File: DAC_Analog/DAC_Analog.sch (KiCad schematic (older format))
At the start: 0 parts

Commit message: Update dac analog design
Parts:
- added U?: ISO154x, symbol ISO154x
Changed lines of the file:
@@
 Text Notes 8550 3900 0    79   ~ 0
 Digital \nsource converter\n &\nDAC
+$Comp
+L ISO154x U?
+U 1 1 59C5CEDC
+P 4850 4050
+F 0 "U?" H 4600 4500 60  0000 C CNN
+F 1 "ISO154x" H 4950 3600 60  0000 C CNN
+F 2 "" H 4850 4050 60  0001 C CNN
+F 3 "" H 4850 4050 60  0001 C CNN
+	1    4850 4050
+	1    0    0    -1
+$EndComp
 $EndSCHEMATC

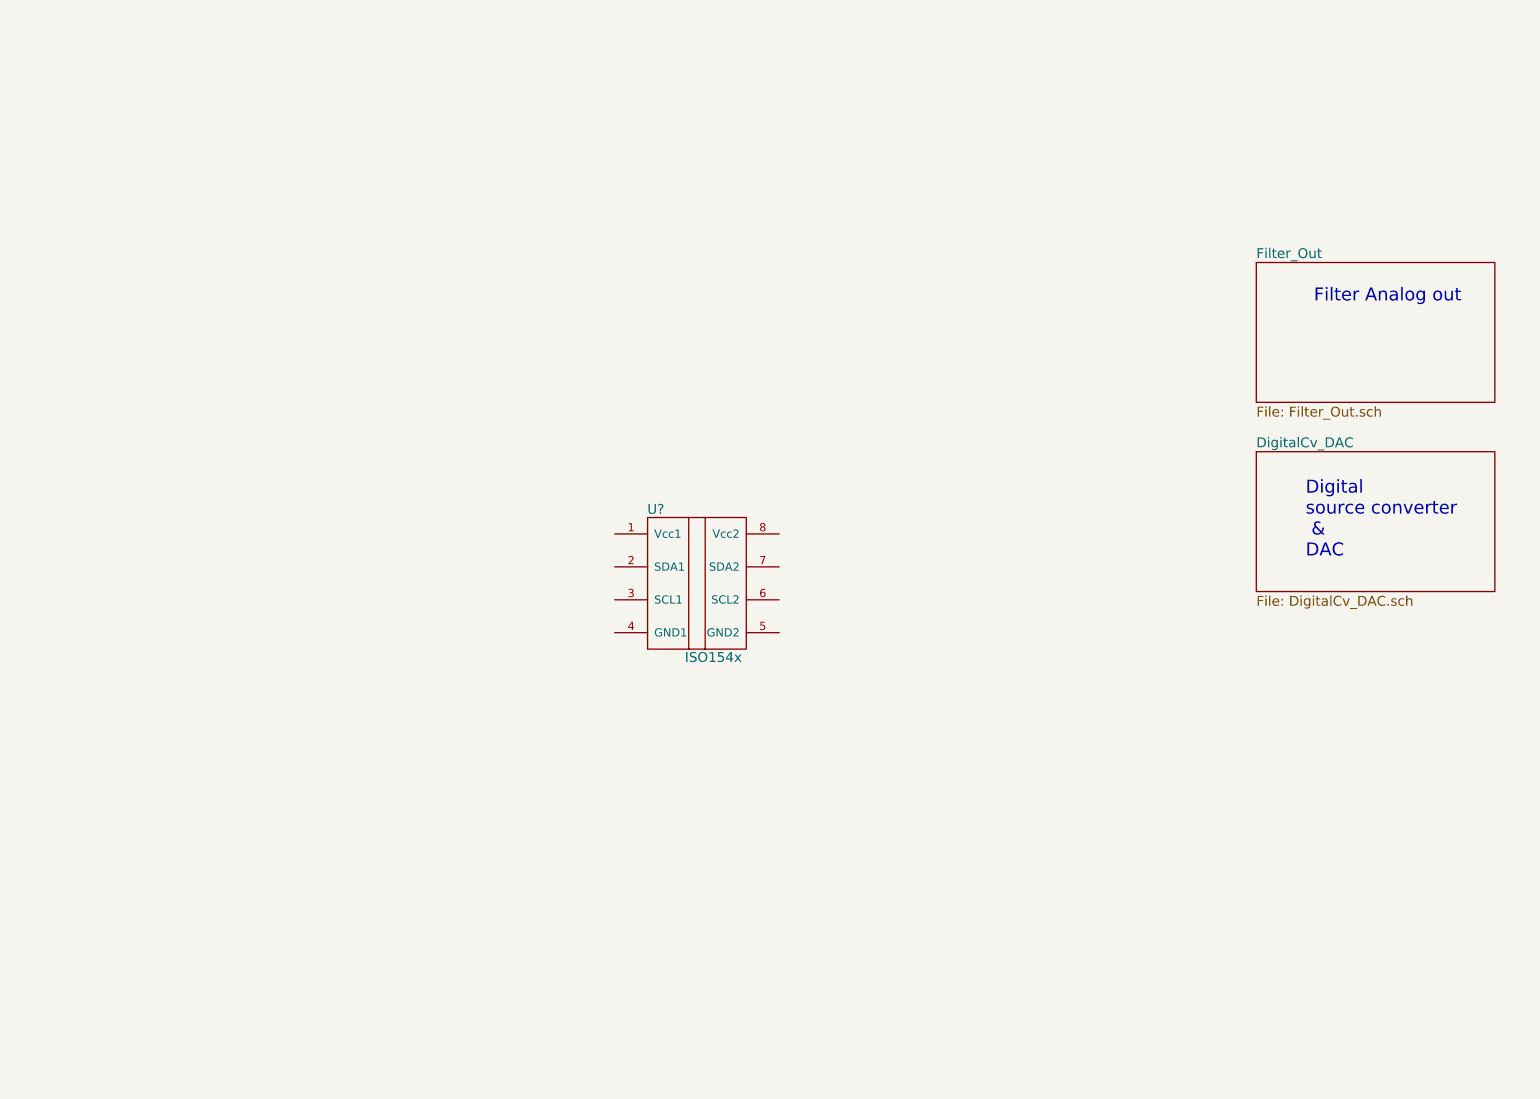
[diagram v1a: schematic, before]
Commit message: Update DAC_analog
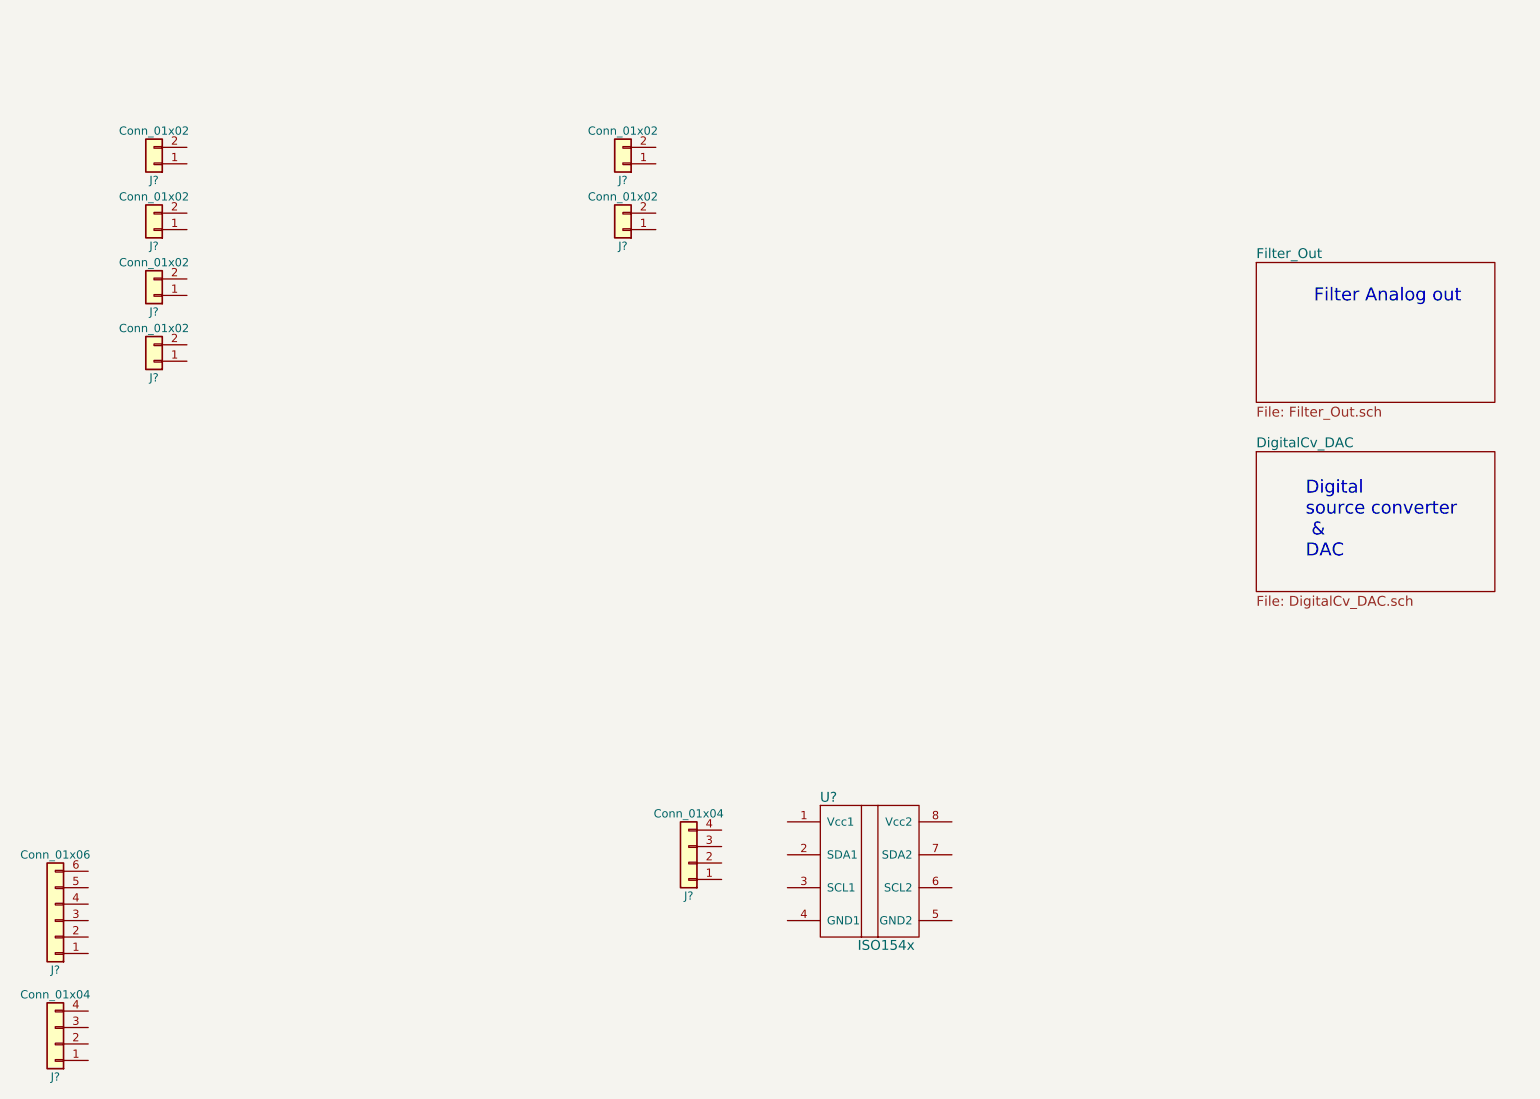
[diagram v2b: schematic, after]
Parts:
- added J? (x6): Conn_01x02, symbol Conn_01x02
- added J? (x2): Conn_01x04, symbol Conn_01x04
- added J?: Conn_01x06, symbol Conn_01x06
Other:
- moved on the sheet: U?
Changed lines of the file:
@@
 L ISO154x U?
 U 1 1 59C5CEDC
-P 4850 4050
-F 0 "U?" H 4600 4500 60  0000 C CNN
-F 1 "ISO154x" H 4950 3600 60  0000 C CNN
-F 2 "" H 4850 4050 60  0001 C CNN
-F 3 "" H 4850 4050 60  0001 C CNN
-	1    4850 4050
+P 5900 5800
+F 0 "U?" H 5650 6250 60  0000 C CNN
+F 1 "ISO154x" H 6000 5350 60  0000 C CNN
+F 2 "" H 5900 5800 60  0001 C CNN
+F 3 "" H 5900 5800 60  0001 C CNN
+	1    5900 5800
 	1    0    0    -1
 $EndComp
+$Comp
+L Conn_01x02 J?
+U 1 1 59C96FBC
+P 1550 1500
+F 0 "J?" H 1550 1600 50  0000 C CNN
+F 1 "Conn_01x02" H 1550 1300 50  0000 C CNN
+F 2 "" H 1550 1500 50  0001 C CNN
+F 3 "" H 1550 1500 50  0001 C CNN
+	1    1550 1500
+	-1   0    0    1
+$EndComp
+$Comp
+L Conn_01x02 J?
+U 1 1 59C970A3
+P 1550 1900
+F 0 "J?" H 1550 2000 50  0000 C CNN
+F 1 "Conn_01x02" H 1550 1700 50  0000 C CNN
+F 2 "" H 1550 1900 50  0001 C CNN
+F 3 "" H 1550 1900 50  0001 C CNN
+	1    1550 1900
+	-1   0    0    1
+$EndComp
+$Comp
+L Conn_01x02 J?
+U 1 1 59C970DE
+P 1550 2300
+F 0 "J?" H 1550 2400 50  0000 C CNN
+F 1 "Conn_01x02" H 1550 2100 50  0000 C CNN
+F 2 "" H 1550 2300 50  0001 C CNN
+F 3 "" H 1550 2300 50  0001 C CNN
+	1    1550 2300
+	-1   0    0    1
+$EndComp
+$Comp
+L Conn_01x02 J?
+U 1 1 59C97110
+P 1550 2700
+F 0 "J?" H 1550 2800 50  0000 C CNN
+F 1 "Conn_01x02" H 1550 2500 50  0000 C CNN
+F 2 "" H 1550 2700 50  0001 C CNN
+F 3 "" H 1550 2700 50  0001 C CNN
+	1    1550 2700
+	-1   0    0    1
+$EndComp
+$Comp
+L Conn_01x04 J?
+U 1 1 59C971D1
+P 950 6850
+F 0 "J?" H 950 7050 50  0000 C CNN
+F 1 "Conn_01x04" H 950 6550 50  0000 C CNN
+F 2 "" H 950 6850 50  0001 C CNN
+F 3 "" H 950 6850 50  0001 C CNN
+	1    950  6850
+	-1   0    0    1
+$EndComp
+$Comp
+L Conn_01x06 J?
+U 1 1 59C972F4
+P 950 6100
+F 0 "J?" H 950 6400 50  0000 C CNN
+F 1 "Conn_01x06" H 950 5700 50  0000 C CNN
+F 2 "" H 950 6100 50  0001 C CNN
+F 3 "" H 950 6100 50  0001 C CNN
+	1    950  6100
+	-1   0    0    1
+$EndComp
+$Comp
+L Conn_01x04 J?
+U 1 1 59C97424
+P 4800 5750
+F 0 "J?" H 4800 5950 50  0000 C CNN
+F 1 "Conn_01x04" H 4800 5450 50  0000 C CNN
+F 2 "" H 4800 5750 50  0001 C CNN
+F 3 "" H 4800 5750 50  0001 C CNN
+	1    4800 5750
+	-1   0    0    1
+$EndComp
+$Comp
+L Conn_01x02 J?
+U 1 1 59C976CC
+P 4400 1500
+F 0 "J?" H 4400 1600 50  0000 C CNN
+F 1 "Conn_01x02" H 4400 1300 50  0000 C CNN
+F 2 "" H 4400 1500 50  0001 C CNN
+F 3 "" H 4400 1500 50  0001 C CNN
+	1    4400 1500
+	-1   0    0    1
+$EndComp
+$Comp
+L Conn_01x02 J?
+U 1 1 59C976D2
+P 4400 1900
+F 0 "J?" H 4400 2000 50  0000 C CNN
+F 1 "Conn_01x02" H 4400 1700 50  0000 C CNN
+F 2 "" H 4400 1900 50  0001 C CNN
+F 3 "" H 4400 1900 50  0001 C CNN
+	1    4400 1900
+	-1   0    0    1
+$EndComp
 $EndSCHEMATC

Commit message: Finish DAC_Analog schematic
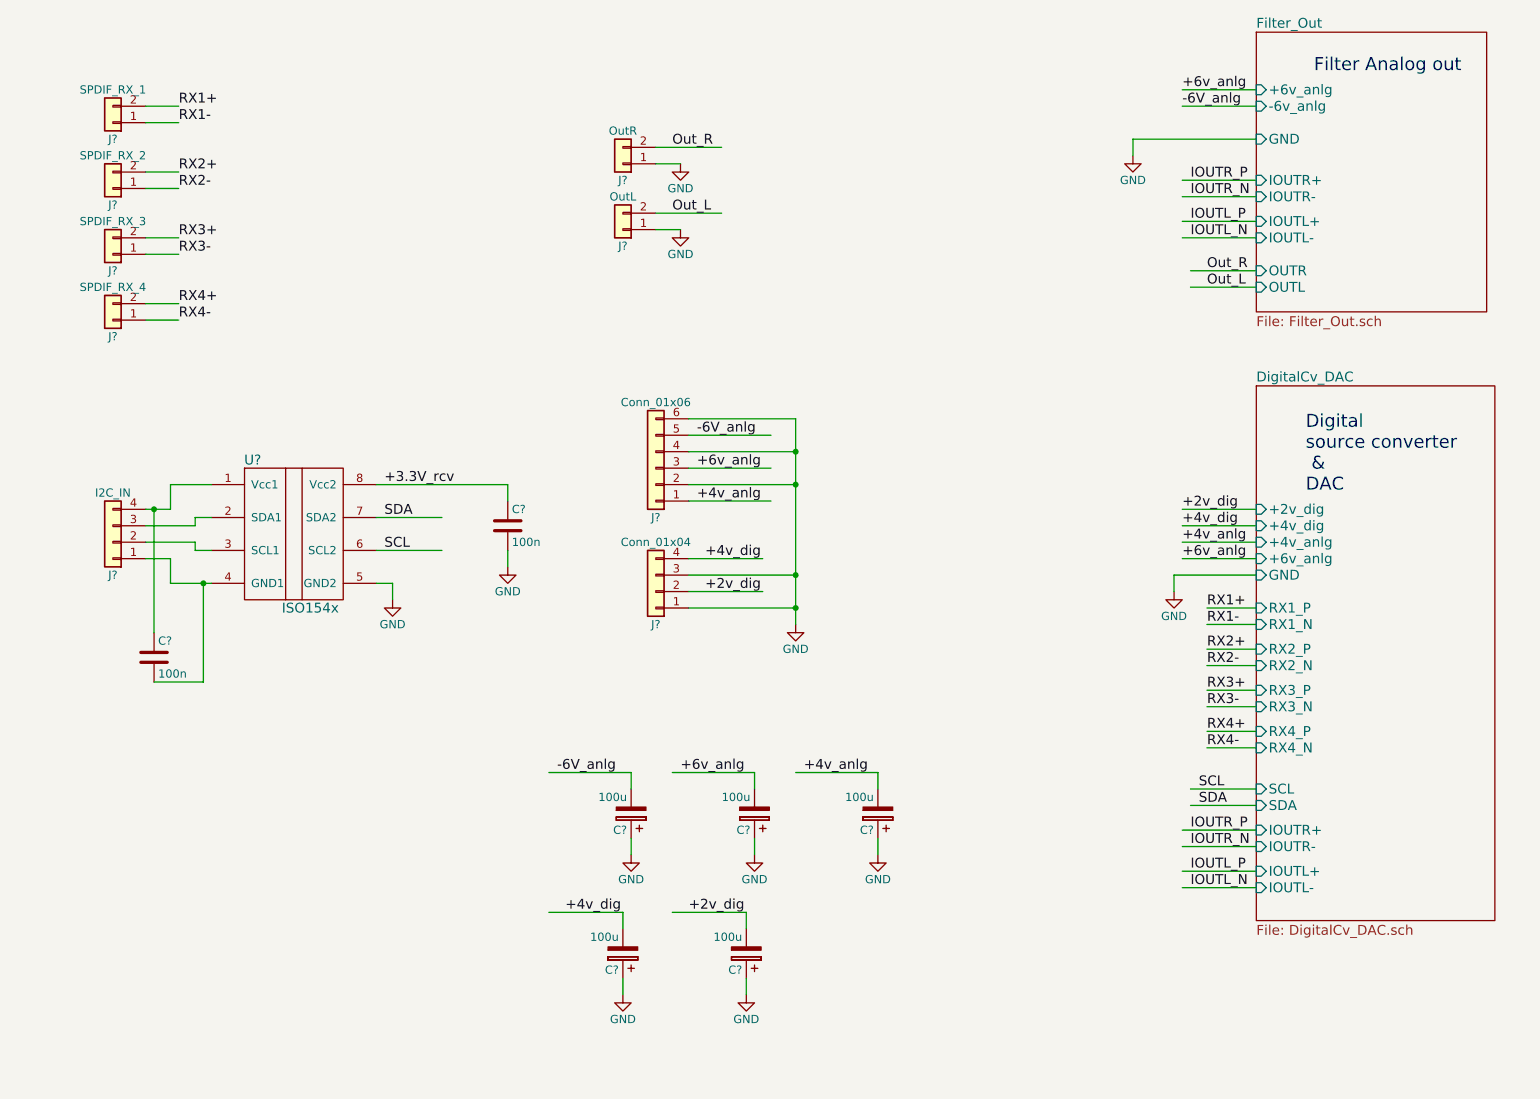
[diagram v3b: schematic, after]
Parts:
- added C? (x2): 100n, symbol C
- added C? (x5): 100u, symbol CP
- J?: value Conn_01x02 -> SPDIF_RX_1
- J?: value Conn_01x02 -> SPDIF_RX_2
- J?: value Conn_01x02 -> SPDIF_RX_3
- J?: value Conn_01x02 -> SPDIF_RX_4
- J?: value Conn_01x04 -> I2C_IN
- J?: value Conn_01x02 -> OutR
- J?: value Conn_01x02 -> OutL
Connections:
- net labels added: +2v_dig, +3.3V_rcv, +4v_anlg, +4v_dig, +6v_anlg, -6V_anlg, GND, IOUTL_N, IOUTL_P, IOUTR_N, IOUTR_P, Out_L, Out_R, RX1+, RX1-, RX2+, RX2-, RX3+, RX3-, RX4+, RX4-, SCL, SDA
- wire segments 0 -> 90
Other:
- moved on the sheet: J?, U?

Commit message: Redo DAC_Analog
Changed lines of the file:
@@
 F 3 "" H 4450 5450 50  0001 C CNN
 	1    4450 5450
-	-1   0    0    1
+	1    0    0    -1
 $EndComp
 $Comp
@@
 F 3 "" H 5200 5450 50  0001 C CNN
 	1    5200 5450
-	-1   0    0    1
+	-1   0    0    -1
 $EndComp
 $Comp
@@
 F 3 "" H 5950 5450 50  0001 C CNN
 	1    5950 5450
-	-1   0    0    1
+	-1   0    0    -1
 $EndComp
 $Comp
@@
 F 3 "" H 5150 6300 50  0001 C CNN
 	1    5150 6300
-	-1   0    0    1
+	-1   0    0    -1
 $EndComp
 $Comp
@@
 F 3 "" H 4400 6300 50  0001 C CNN
 	1    4400 6300
-	-1   0    0    1
+	-1   0    0    -1
 $EndComp
 $Comp

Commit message: set DAC_Analog footprint
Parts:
- C? (x2): footprint (none) -> Yame_library:SM0603-MR
- C? (x5): footprint (none) -> Capacitors_THT:CP_Radial_Tantal_D8.0mm_P2.50mm
- J? (x2): footprint (none) -> Yame_library:HE10_14-4C-2.54-MR
- J?: footprint (none) -> Yame_library:HE10_14-6C-2.54-MR
- J?: footprint (none) -> Housings_DIP:DIP-6_W10.16mm_LongPads
- J?: footprint (none) -> Yame_library:HE10_14-2C-2.54-MR
- U?: footprint (none) -> Housings_SOIC:SOIC-8_3.9x4.9mm_Pitch1.27mm
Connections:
- wire segments 90 -> 91
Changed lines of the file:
@@
 Text Notes 8600 950  0    79   ~ 0
 Filter Analog out
-$Sheet
-S 8250 2850 1450 3250
-U 599B5101
-F0 "DigitalCv_DAC" 60
-F1 "DigitalCv_DAC.sch" 60
-F2 "RX1_P" I L 8250 4200 60
-F3 "RX1_N" I L 8250 4300 60
-F4 "RX2_P" I L 8250 4450 60
-F5 "RX2_N" I L 8250 4550 60
-F6 "RX3_P" I L 8250 4700 60
-F7 "RX3_N" I L 8250 4800 60
-F8 "RX4_P" I L 8250 4950 60
-F9 "RX4_N" I L 8250 5050 60
-F10 "+4v_dig" I L 8250 3700 60
-F11 "+2v_dig" I L 8250 3600 60
-F12 "+4v_anlg" I L 8250 3800 60
-F13 "+6v_anlg" I L 8250 3900 60
-F14 "GND" I L 8250 4000 60
-F15 "SCL" I L 8250 5300 60
-F16 "SDA" I L 8250 5400 60
-F17 "IOUTR+" I L 8250 5550 60
-F18 "IOUTR-" I L 8250 5650 60
-F19 "IOUTL+" I L 8250 5800 60
-F20 "IOUTL-" I L 8250 5900 60
-$EndSheet
-Text Notes 8550 3500 0    79   ~ 0
+Text Notes 8650 3350 0    79   ~ 0
 Digital \nsource converter\n &\nDAC
 $Comp
@@
 F 0 "U?" H 2150 4200 60  0000 C CNN
 F 1 "ISO154x" H 2500 3300 60  0000 C CNN
-F 2 "" H 2400 3750 60  0001 C CNN
+F 2 "Housings_SOIC:SOIC-8_3.9x4.9mm_Pitch1.27mm" H 2400 3750 60  0001 C CNN
 F 3 "" H 2400 3750 60  0001 C CNN
 	1    2400 3750
@@
 F 0 "J?" H 4600 4300 50  0000 C CNN
 F 1 "Conn_01x04" H 4600 3800 50  0000 C CNN
-F 2 "" H 4600 4100 50  0001 C CNN
+F 2 "Yame_library:HE10_14-4C-2.54-MR" H 4600 4100 50  0001 C CNN
 F 3 "" H 4600 4100 50  0001 C CNN
 	1    4600 4100
@@
 F 0 "J?" H 4600 3650 50  0000 C CNN
 F 1 "Conn_01x06" H 4600 2950 50  0000 C CNN
-F 2 "" H 4600 3350 50  0001 C CNN
+F 2 "Yame_library:HE10_14-6C-2.54-MR" H 4600 3350 50  0001 C CNN
 F 3 "" H 4600 3350 50  0001 C CNN
 	1    4600 3350
@@
 F 0 "J?" H 1300 4000 50  0000 C CNN
 F 1 "I2C_IN" H 1300 3500 50  0000 C CNN
-F 2 "" H 1300 3800 50  0001 C CNN
+F 2 "Yame_library:HE10_14-4C-2.54-MR" H 1300 3800 50  0001 C CNN
 F 3 "" H 1300 3800 50  0001 C CNN
 	1    1300 3800
@@
 F 0 "J?" H 4400 1600 50  0000 C CNN
 F 1 "OutR" H 4400 1300 50  0000 C CNN
-F 2 "" H 4400 1500 50  0001 C CNN
+F 2 "Housings_DIP:DIP-6_W10.16mm_LongPads" H 4400 1500 50  0001 C CNN
 F 3 "" H 4400 1500 50  0001 C CNN
 	1    4400 1500
@@
 F 0 "J?" H 4400 2000 50  0000 C CNN
 F 1 "OutL" H 4400 1700 50  0000 C CNN
-F 2 "" H 4400 1900 50  0001 C CNN
+F 2 "Yame_library:HE10_14-2C-2.54-MR" H 4400 1900 50  0001 C CNN
 F 3 "" H 4400 1900 50  0001 C CNN
 	1    4400 1900
@@
 Wire Wire Line
 	4600 1900 4750 1900
-Text Label 7800 3800 0    60   ~ 0
+Text Label 7800 3650 0    60   ~ 0
 +4v_anlg
-Text Label 7800 3900 0    60   ~ 0
+Text Label 7800 3750 0    60   ~ 0
 +6v_anlg
 Wire Wire Line
-	7800 3800 8250 3800
-Wire Wire Line
-	7800 3900 8250 3900
-Text Label 7800 3700 0    60   ~ 0
+	7800 3650 8250 3650
+Wire Wire Line
+	7800 3750 8250 3750
+Text Label 7800 3550 0    60   ~ 0
 +4v_dig
-Text Label 7800 3600 0    60   ~ 0
+Text Label 7800 3450 0    60   ~ 0
 +2v_dig
 Wire Wire Line
-	7800 3700 8250 3700
-Wire Wire Line
-	7800 3600 8250 3600
+	7800 3550 8250 3550
+Wire Wire Line
+	7800 3450 8250 3450
 Text Label 4900 3900 0    60   ~ 0
 +4v_dig
@@
 F 0 "C?" H 3725 3800 50  0000 L CNN
 F 1 "100n" H 3725 3600 50  0000 L CNN
-F 2 "" H 3738 3550 50  0001 C CNN
+F 2 "Yame_library:SM0603-MR" H 3738 3550 50  0001 C CNN
 F 3 "" H 3700 3700 50  0001 C CNN
 	1    3700 3700
@@
 F 0 "C?" H 1575 4600 50  0000 L CNN
 F 1 "100n" H 1575 4400 50  0000 L CNN
-F 2 "" H 1588 4350 50  0001 C CNN
+F 2 "Yame_library:SM0603-MR" H 1588 4350 50  0001 C CNN
 F 3 "" H 1550 4500 50  0001 C CNN
 	1    1550 4500
@@
 F 0 "C?" H 4475 5550 50  0000 L CNN
 F 1 "100u" H 4475 5350 50  0000 L CNN
-F 2 "" H 4488 5300 50  0001 C CNN
+F 2 "Capacitors_THT:CP_Radial_Tantal_D8.0mm_P2.50mm" H 4488 5300 50  0001 C CNN
 F 3 "" H 4450 5450 50  0001 C CNN
 	1    4450 5450
@@
 F 0 "C?" H 5225 5550 50  0000 L CNN
 F 1 "100u" H 5225 5350 50  0000 L CNN
-F 2 "" H 5238 5300 50  0001 C CNN
+F 2 "Capacitors_THT:CP_Radial_Tantal_D8.0mm_P2.50mm" H 5238 5300 50  0001 C CNN
 F 3 "" H 5200 5450 50  0001 C CNN
 	1    5200 5450
@@
 F 0 "C?" H 5975 5550 50  0000 L CNN
 F 1 "100u" H 5975 5350 50  0000 L CNN
-F 2 "" H 5988 5300 50  0001 C CNN
+F 2 "Capacitors_THT:CP_Radial_Tantal_D8.0mm_P2.50mm" H 5988 5300 50  0001 C CNN
 F 3 "" H 5950 5450 50  0001 C CNN
 	1    5950 5450
@@
 F 0 "C?" H 5175 6400 50  0000 L CNN
 F 1 "100u" H 5175 6200 50  0000 L CNN
-F 2 "" H 5188 6150 50  0001 C CNN
+F 2 "Capacitors_THT:CP_Radial_Tantal_D8.0mm_P2.50mm" H 5188 6150 50  0001 C CNN
 F 3 "" H 5150 6300 50  0001 C CNN
 	1    5150 6300
@@
 F 0 "C?" H 4425 6400 50  0000 L CNN
 F 1 "100u" H 4425 6200 50  0000 L CNN
-F 2 "" H 4438 6150 50  0001 C CNN
+F 2 "Capacitors_THT:CP_Radial_Tantal_D8.0mm_P2.50mm" H 4438 6150 50  0001 C CNN
 F 3 "" H 4400 6300 50  0001 C CNN
 	1    4400 6300
@@
 Wire Wire Line
 	4400 6450 4400 6550
+$Sheet
+S 8250 2850 1450 3250
+U 599B5101
+F0 "DigitalCv_DAC" 60
+F1 "DigitalCv_DAC.sch" 60
+F2 "+2v_dig" I L 8250 3450 60
+F3 "+4v_dig" I L 8250 3550 60
+F4 "+4v_anlg" I L 8250 3650 60
+F5 "+6v_anlg" I L 8250 3750 60
+F6 "+3.3V_rcv" I L 8250 3850 60
+F7 "RX1+" I L 8250 4200 60
+F8 "RX1-" I L 8250 4300 60
+F9 "RX2+" I L 8250 4450 60
+F10 "RX2-" I L 8250 4550 60
+F11 "RX3+" I L 8250 4700 60
+F12 "RX3-" I L 8250 4800 60
+F13 "RX4+" I L 8250 4950 60
+F14 "RX4-" I L 8250 5050 60
+F15 "SCL" I L 8250 5300 60
+F16 "SDA" I L 8250 5400 60
+F17 "IOUTR_P" I L 8250 5550 60
+F18 "IOUTR_N" I L 8250 5650 60
+F19 "IOUTL_P" I L 8250 5800 60
+F20 "IOUTL_N" I L 8250 5900 60
+F21 "GND" I L 8250 4000 60
+$EndSheet
+Text Label 7750 3850 0    60   ~ 0
++3.3V_rcv
+Wire Wire Line
+	7750 3850 8250 3850
 $EndSCHEMATC
